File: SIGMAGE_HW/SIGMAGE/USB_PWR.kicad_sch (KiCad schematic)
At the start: 36 parts, among them J1 UJ31CHG2SMTTR, J14 HTSW10807GD, J15 HTSW10807GD, J16 HTSW10807GD, J17 HTSW10807GD, J18 HTSW10107GD, J19 HTSW10107GD, U1 MAX8902BATA/V+T, U2 MAX8902BATA/V+T

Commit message: some schematic adjustments
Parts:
- removed J14, J15, J16, J17: HTSW10807GD, SIGMAGE:HTSW10807GD, symbol SIGMAGE:HTSW10807GD

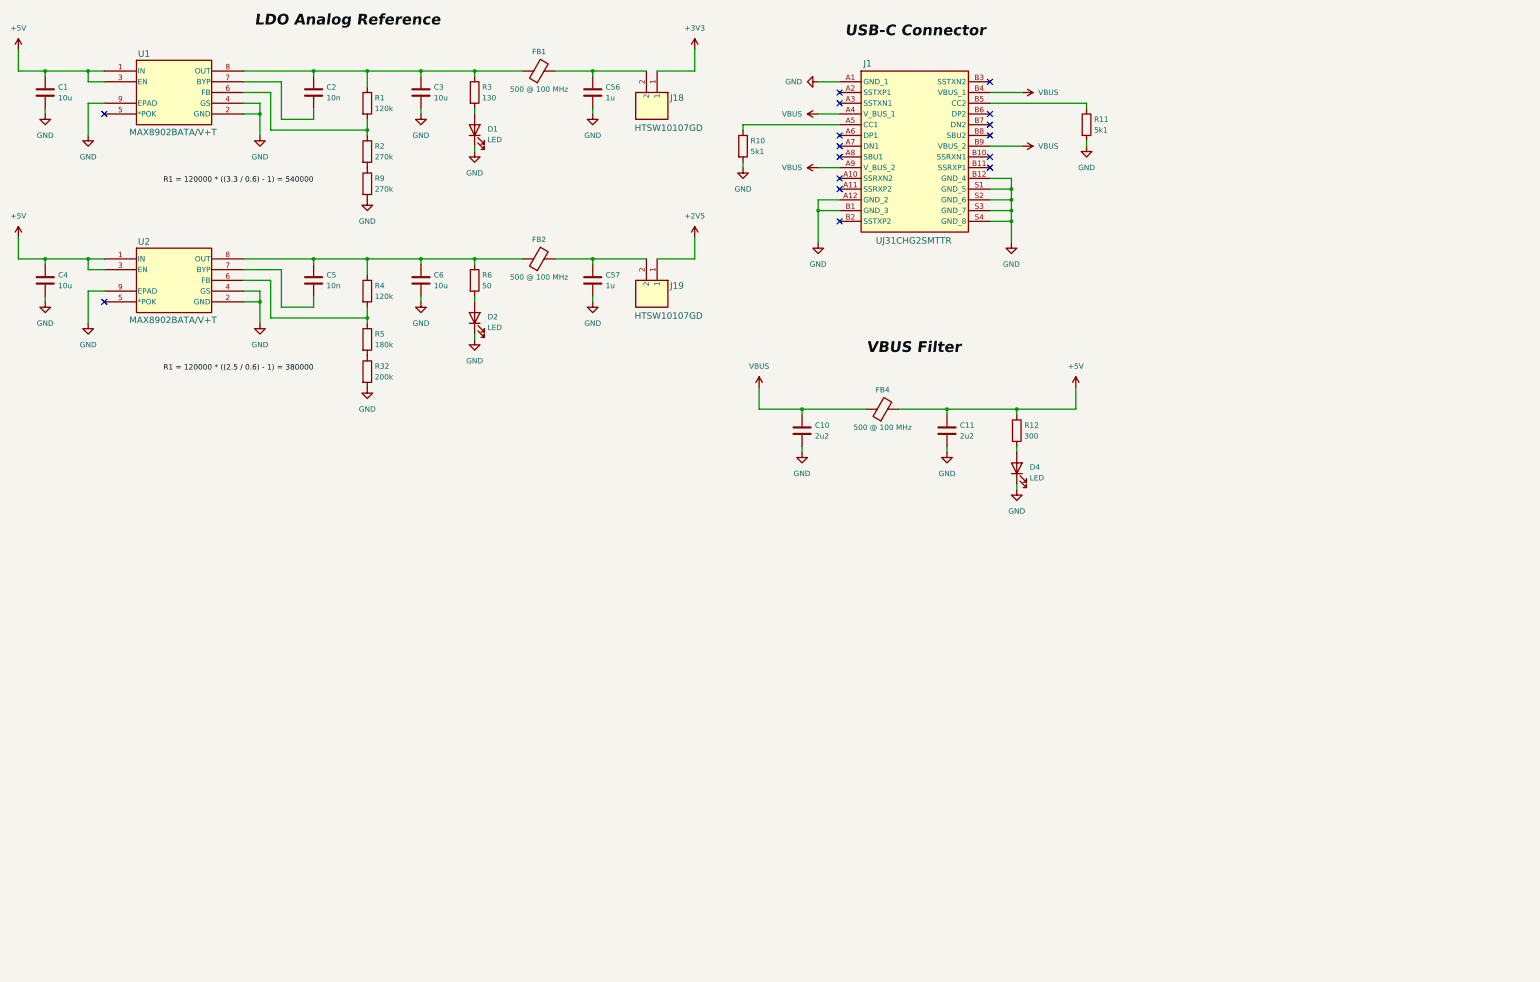
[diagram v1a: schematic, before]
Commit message: added TPS62130RGTT and added digital/analog converter
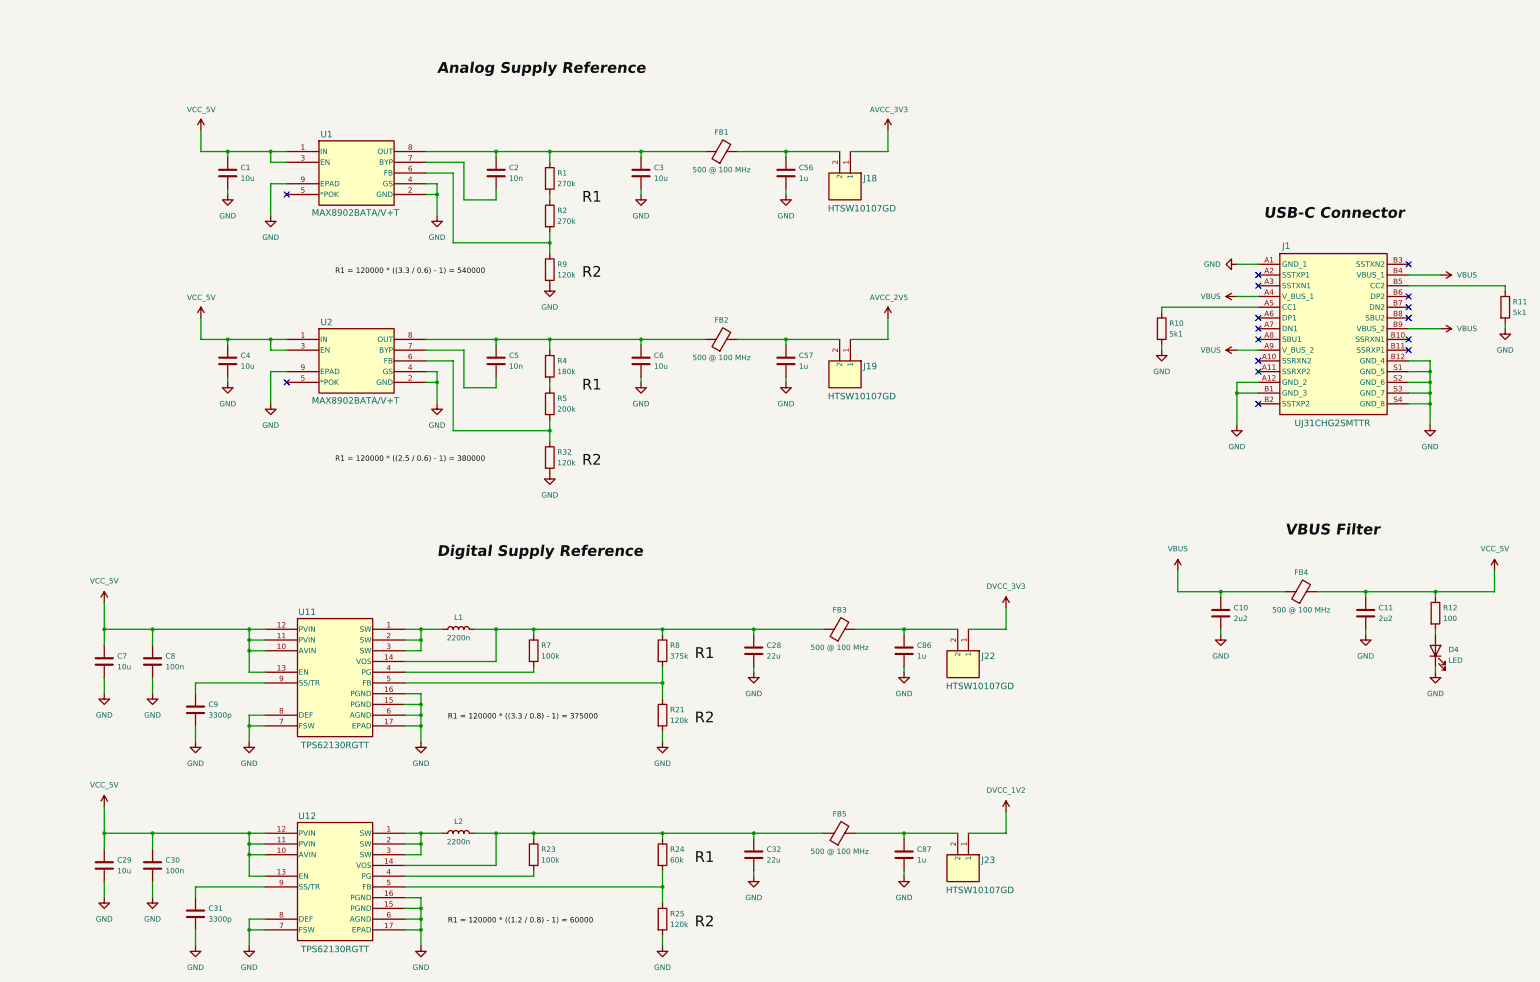
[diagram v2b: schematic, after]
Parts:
- removed D1, D2: LED, LED_SMD:LED_0603_1608Metric, symbol Device:LED
- removed R3: 130, Resistor_SMD:R_0603_1608Metric, symbol Device:R
- removed R6: 50, Resistor_SMD:R_0603_1608Metric, symbol Device:R
- added C28, C32: 22u, Capacitor_SMD:C_0603_1608Metric, symbol Device:C
- added C29, C7: 10u, Capacitor_SMD:C_0603_1608Metric, symbol Device:C
- added C30, C8: 100n, Capacitor_SMD:C_0603_1608Metric, symbol Device:C
- added C31, C9: 3300p, Capacitor_SMD:C_0603_1608Metric, symbol Device:C
- added C86, C87: 1u, Capacitor_SMD:C_0603_1608Metric, symbol Device:C
- added FB3, FB5: 500 @ 100 MHz, Capacitor_SMD:C_0603_1608Metric, symbol Device:FerriteBead
- added J22, J23: HTSW10107GD, SIGMAGE:HTSW10107GD, symbol SIGMAGE:HTSW10107GD
- added L1, L2: 2200n, symbol Device:L
- added R21, R25: 120k, Resistor_SMD:R_0603_1608Metric, symbol Device:R
- added R23, R7: 100k, Resistor_SMD:R_0603_1608Metric, symbol Device:R
- added R24: 60k, Resistor_SMD:R_0603_1608Metric, symbol Device:R
- added R8: 375k, Resistor_SMD:R_0603_1608Metric, symbol Device:R
- added U11, U12: TPS62130RGTT, SIGMAGE:TPS62130RGTT, symbol SIGMAGE:TPS62130RGTT
- R1: value 120k -> 270k
- R12: value 300 -> 100
- R32: value 200k -> 120k
- R4: value 120k -> 180k
- R5: value 180k -> 200k
- R9: value 270k -> 120k
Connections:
- net GND: now also C28.2, C29.2, C30.2, C31.2, C32.2, C7.2, C8.2, C86.2, C87.2, C9.2, R21.2, R25.2, U11.15 (PGND), U11.16 (PGND), U11.17 (EPAD), U11.6 (AGND), U11.7 (FSW), U11.8 (DEF), U12.15 (PGND), U12.16 (PGND), U12.17 (EPAD), U12.6 (AGND), U12.7 (FSW), U12.8 (DEF)
- net at R32.1, R5.2: now also U2.6 (FB)
- net at R1.2, R2.1: no longer U1.6 (FB)
- net at R4.2, R5.1: no longer U2.6 (FB)
- net at R2.2, R9.1: now also U1.6 (FB)
- net +2V5 renamed AVCC_2V5
- net +3V3 renamed AVCC_3V3
- net +5V renamed VCC_5V
- net VCC_5V: now also C29.1, C30.1, C7.1, C8.1, U11.10 (AVIN), U11.11 (PVIN), U11.12 (PVIN), U11.13 (EN), U12.10 (AVIN), U12.11 (PVIN), U12.12 (PVIN), U12.13 (EN)
- new net: C87.1, FB5.2, J23.2
- new net: C32.1, FB5.1, L2.2, R23.1, R24.1, U12.14 (VOS)
- new net: R24.2, R25.1, U12.5 (FB)
- new net: C31.1, U12.9 (SS/TR)
- new net: C86.1, FB3.2, J22.2
- new net: L1.1, U11.1 (SW), U11.2 (SW), U11.3 (SW)
- new net: C28.1, FB3.1, L1.2, R7.1, R8.1, U11.14 (VOS)
- new net: C9.1, U11.9 (SS/TR)
- new net: L2.1, U12.1 (SW), U12.2 (SW), U12.3 (SW)
- new net: R7.2, U11.4 (PG)
- new net: R21.1, R8.2, U11.5 (FB)
- new net: R23.2, U12.4 (PG)
- new net DVCC_1V2: J23.1
- new net DVCC_3V3: J22.1
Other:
- moved on the sheet: C1, C10, C11, C2, C3, C4, C5, C56, C57, C6, D4, FB1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

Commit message: some USB interface
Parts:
- removed C1, C29, C3, C4, C6, C7: 10u, Capacitor_SMD:C_0603_1608Metric, symbol Device:C
- removed C10, C11: 2u2, Capacitor_SMD:C_0603_1608Metric, symbol Device:C
- removed C2, C5: 10n, Capacitor_SMD:C_0603_1608Metric, symbol Device:C
- removed C28, C32: 22u, Capacitor_SMD:C_0603_1608Metric, symbol Device:C
- removed C30, C8: 100n, Capacitor_SMD:C_0603_1608Metric, symbol Device:C
- removed C31, C9: 3300p, Capacitor_SMD:C_0603_1608Metric, symbol Device:C
- removed C56, C57, C86, C87: 1u, Capacitor_SMD:C_0603_1608Metric, symbol Device:C
- removed D4: LED, LED_SMD:LED_0603_1608Metric, symbol Device:LED
- removed FB1, FB2, FB3, FB4, FB5: 500 @ 100 MHz, Capacitor_SMD:C_0603_1608Metric, symbol Device:FerriteBead
- removed J1: UJ31CHG2SMTTR, SIGMAGE:UJ31CHG2SMTTR, symbol SIGMAGE:UJ31CHG2SMTTR
- removed J18, J19, J22, J23: HTSW10107GD, SIGMAGE:HTSW10107GD, symbol SIGMAGE:HTSW10107GD
- removed L1, L2: 2200n, symbol Device:L
- removed R1, R2: 270k, Resistor_SMD:R_0603_1608Metric, symbol Device:R
- removed R10, R11: 5k1, Resistor_SMD:R_0603_1608Metric, symbol Device:R
- removed R12: 100, Resistor_SMD:R_0603_1608Metric, symbol Device:R
- removed R21, R25, R32, R9: 120k, Resistor_SMD:R_0603_1608Metric, symbol Device:R
- removed R23, R7: 100k, Resistor_SMD:R_0603_1608Metric, symbol Device:R
- removed R24: 60k, Resistor_SMD:R_0603_1608Metric, symbol Device:R
- removed R4: 180k, Resistor_SMD:R_0603_1608Metric, symbol Device:R
- removed R5: 200k, Resistor_SMD:R_0603_1608Metric, symbol Device:R
- removed R8: 375k, Resistor_SMD:R_0603_1608Metric, symbol Device:R
- removed U1, U2: MAX8902BATA/V+T, SIGMAGE:MAX8902BATAVT, symbol SIGMAGE:MAX8902BATAVT
- removed U11, U12: TPS62130RGTT, SIGMAGE:TPS62130RGTT, symbol SIGMAGE:TPS62130RGTT
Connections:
- no-connect marks 16 -> 0
